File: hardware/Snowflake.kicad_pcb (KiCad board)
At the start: 2 copper layers, 70.5 x 79.8 mm, 41 parts, among them J1 Jumper, Q1 Q_DUAL_NMOS, SW1 SW_SPST, U1 Opamp_Single, U2 74HC595, U3 LM4041_1.2V

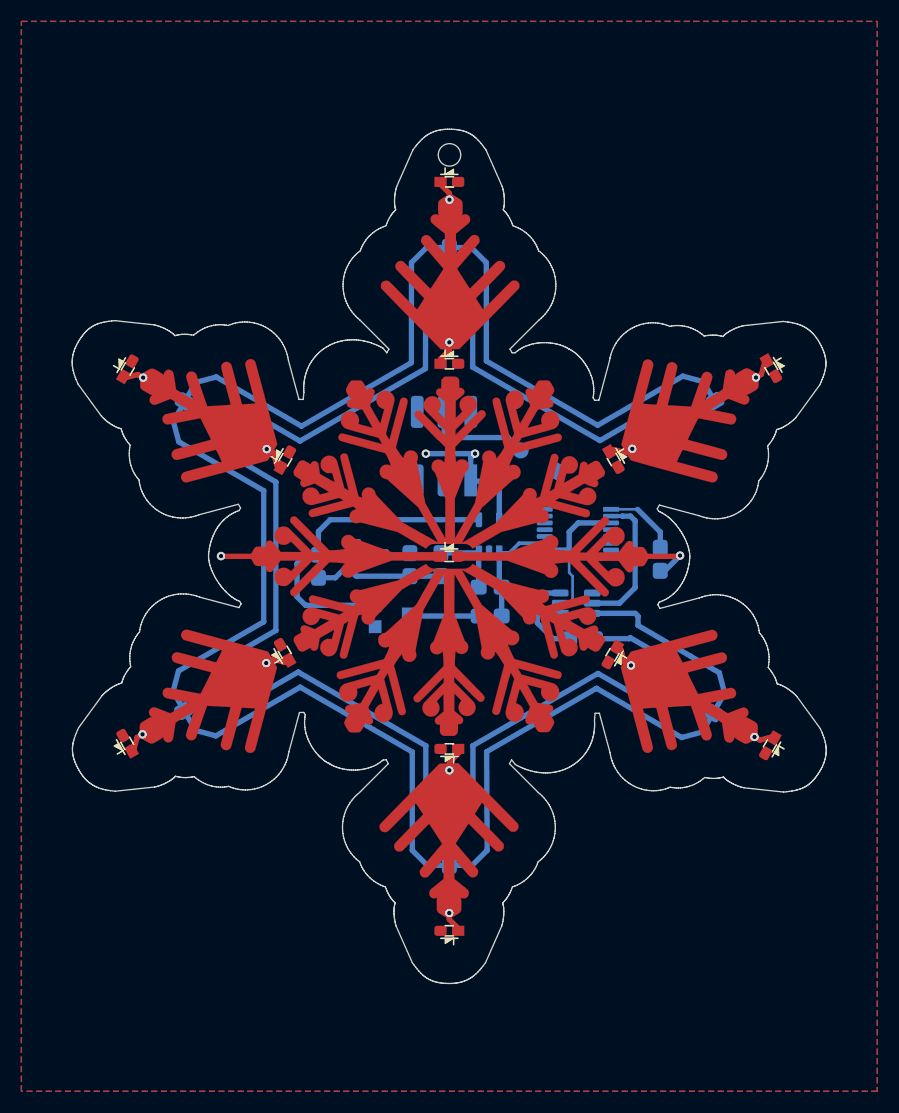
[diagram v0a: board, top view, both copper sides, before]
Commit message: Updated the Design to KiCad6 and made the track corners rounded
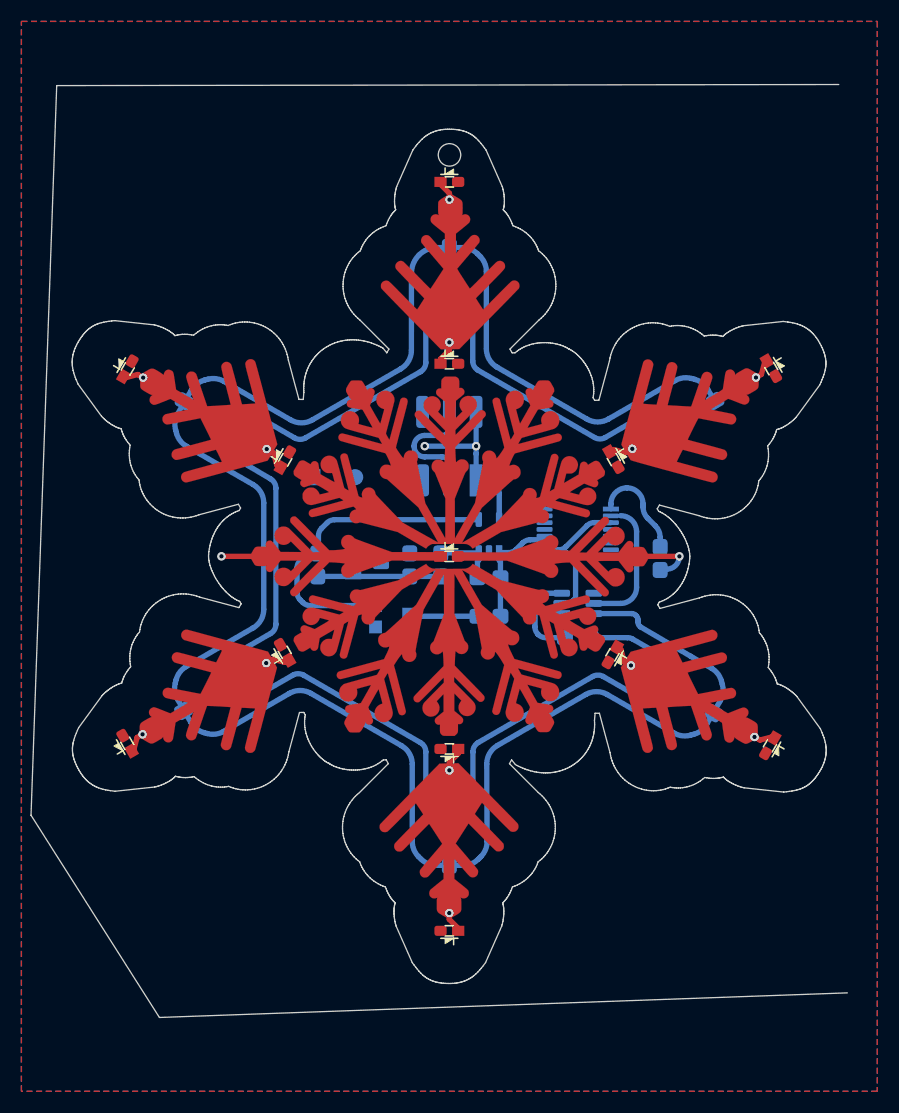
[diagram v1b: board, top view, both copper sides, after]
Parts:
- moved BT1 19.3 mm to (119.2, 109.6), turned to 180 degrees
- moved U3 1.07 mm to (122.3, 117.8)
- moved R2 0.88 mm to (133.7, 119.0)
- moved SW1 0.50 mm to (130.0, 106.7)
- moved J1 0.41 mm to (142.0, 124.6)
- moved C1 0.14 mm to (117.7, 117.8)
- moved Q1 0.14 mm to (142.0, 121.4)
- moved R1 0.11 mm to (133.7, 122.6)
- moved R4 0.08 mm to (149.7, 117.2)
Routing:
- net ROW1: track 211.0 -> 206.3 mm
- net VBAT: track 17.7 -> 21.0 mm
- net LED0: track 6.95 -> 9.61 mm
- net ROW0: track 169.4 -> 167.4 mm
- net Net-(BT1-Pad1): track 9.75 -> 11.4 mm
- net VBIAS: track 13.0 -> 11.6 mm
- net DRIVE_ROW0: track 14.2 -> 13.2 mm
- net Net-(R2-Pad2): track 6.77 -> 6.00 mm
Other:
- board size 70.5 x 79.8 mm -> 76.3 x 87.2 mm
- net class Default removed

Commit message: Fixed a bug, where I was sorting all the LEDs :S Removed all DRC rules Ready to fillet tracks
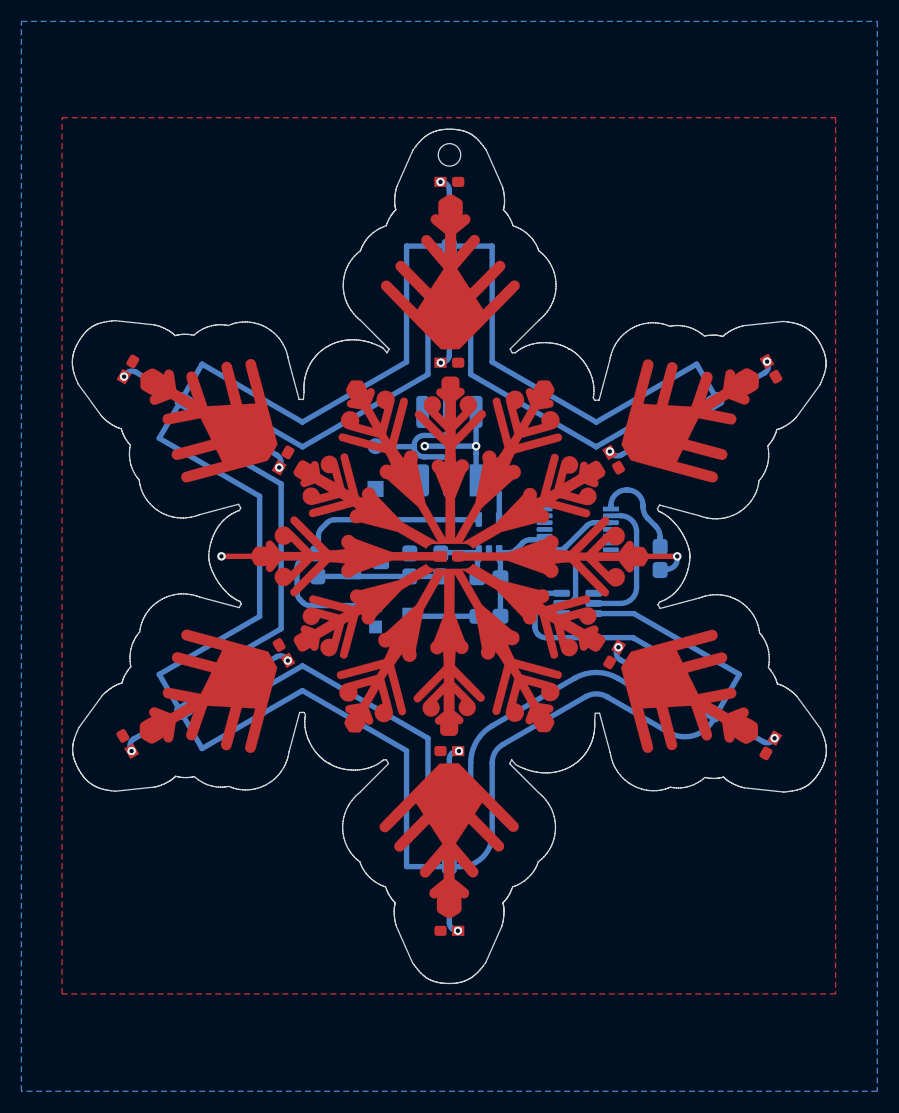
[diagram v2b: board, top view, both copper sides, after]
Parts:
- removed J1: Jumper, Snowflake:Jumper-0805
- BT1: value Battery -> Battery_Cell
- D1: renamed from D3; value White -> LED_Small_ALT; footprint Snowflake:0603_LED_HandSolder -> Snowflake:0603_LED_HandSolder_No_Silk
- D10: renamed from D17; value White -> LED_Small_ALT; footprint Snowflake:0603_LED_HandSolder -> Snowflake:0603_LED_HandSolder_No_Silk
- D11: renamed from D18; value White -> LED_Small_ALT; footprint Snowflake:0603_LED_HandSolder -> Snowflake:0603_LED_HandSolder_No_Silk
- D12: renamed from D21; value White -> LED_Small_ALT; footprint Snowflake:0603_LED_HandSolder -> Snowflake:0603_LED_HandSolder_No_Silk
- D13: renamed from D22; value White -> LED_Small_ALT; footprint Snowflake:0603_LED_HandSolder -> Snowflake:0603_LED_HandSolder_No_Silk
- D2: renamed from D1; value White -> LED_Small_ALT; footprint Snowflake:0603_LED_HandSolder -> Snowflake:0603_LED_HandSolder_No_Silk
- D3: renamed from D2; value White -> LED_Small_ALT; footprint Snowflake:0603_LED_HandSolder -> Snowflake:0603_LED_HandSolder_No_Silk
- D4: renamed from D5; value White -> LED_Small_ALT; footprint Snowflake:0603_LED_HandSolder -> Snowflake:0603_LED_HandSolder_No_Silk
- D5: renamed from D6; value White -> LED_Small_ALT; footprint Snowflake:0603_LED_HandSolder -> Snowflake:0603_LED_HandSolder_No_Silk
- D6: renamed from D9; value White -> LED_Small_ALT; footprint Snowflake:0603_LED_HandSolder -> Snowflake:0603_LED_HandSolder_No_Silk
- D7: renamed from D10; value White -> LED_Small_ALT; footprint Snowflake:0603_LED_HandSolder -> Snowflake:0603_LED_HandSolder_No_Silk
- D8: renamed from D13; value White -> LED_Small_ALT; footprint Snowflake:0603_LED_HandSolder -> Snowflake:0603_LED_HandSolder_No_Silk
- D9: renamed from D14; value White -> LED_Small_ALT; footprint Snowflake:0603_LED_HandSolder -> Snowflake:0603_LED_HandSolder_No_Silk
- R1: renamed from R5; value 6.8kΩ -> R_Small
- R10: renamed from R15; value XYZΩ -> R_Small
- R11: renamed from R16; value XYZΩ -> R_Small
- R12: renamed from R19; value XYZΩ -> R_Small
- R13: renamed from R20; value XYZΩ -> R_Small
- R14: renamed from R23; value XYZΩ -> R_Small
- R15: renamed from R24; value XYZΩ -> R_Small
- R16: renamed from R27; value XYZΩ -> R_Small
- R17: renamed from R28; value XYZΩ -> R_Small
- R2: renamed from R1; value 50kΩ -> R_Small
- R3: renamed from R2; value 35kΩ -> R_Small
- R4: renamed from R3; value 30kΩ -> R_Small
- R5: renamed from R4; value XYZΩ -> R_Small
- R6: renamed from R7; value XYZΩ -> R_Small
- R7: renamed from R8; value XYZΩ -> R_Small
- R8: renamed from R11; value XYZΩ -> R_Small
- R9: renamed from R12; value XYZΩ -> R_Small
- RV1: value 200kΩ -> R_POT_Small
- U1: value Opamp_Single -> Opamp_Single_MCP6001
- U2: renamed from U3; value LM4041_1.2V -> TL431D
- moved BT1 4.00 mm to (123.1, 108.7), turned to -90 degrees
- moved D8 0.20 mm to (130.0, 135.2)
- moved D12 0.16 mm to (114.5, 108.0)
- moved D6 0.16 mm to (145.4, 126.2)
- moved D10 0.11 mm to (114.5, 126.0)
- moved D2 0.10 mm to (130.0, 98.9)
- moved D13 0.06 mm to (100.0, 99.5)
- moved D4 0.06 mm to (145.4, 108.0)
- moved D5 0.05 mm to (160.1, 99.5)
- renumbered U2 to U3
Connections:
- RV1 pad 1: (no net) -> unconnected-(RV1-Pad1)
- U2 pad 3: (no net) -> unconnected-(U2-Pad3)
- U3 pad 10: DRIVE_ROW1 -> RESET
- U3 pad 15: (no net) -> unconnected-(U3-Pad15)
- U3 pad 4: (no net) -> unconnected-(U3-Pad4)
- U3 pad 5: (no net) -> unconnected-(U3-Pad5)
- U3 pad 6: (no net) -> unconnected-(U3-Pad6)
- U3 pad 7: (no net) -> unconnected-(U3-Pad7)
- U3 pad 9: (no net) -> unconnected-(U3-Pad9)
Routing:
- net ROW1: track 206.3 -> 220.8 mm
- net ROW0: track 167.4 -> 178.5 mm
- net Net-(BT1-Pad1): track 11.4 -> 15.1 mm
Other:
- board size 76.3 x 87.2 mm -> 70.5 x 79.8 mm

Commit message: Rounded the tracks!
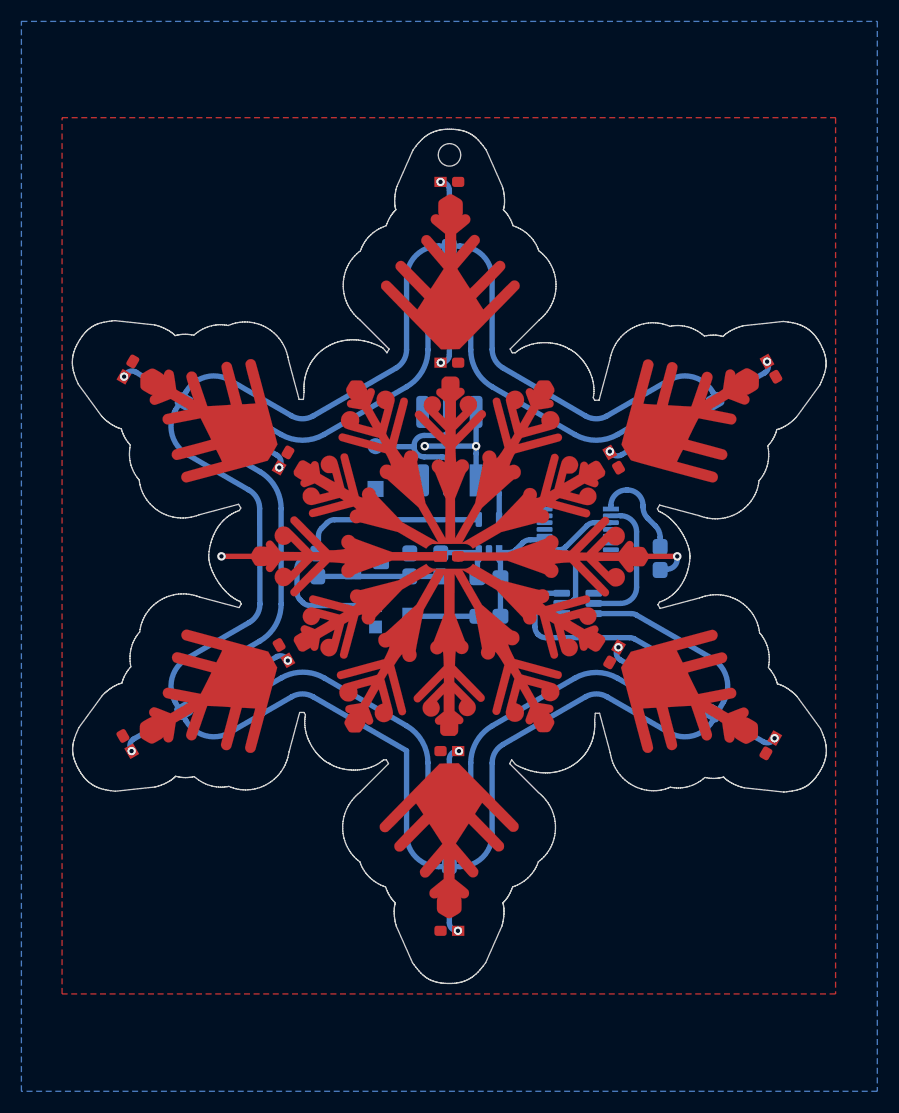
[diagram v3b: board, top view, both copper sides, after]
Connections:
- U3 pad 10: RESET -> DRIVE_ROW1
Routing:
- net ROW1: track 220.8 -> 206.5 mm
- net ROW0: track 178.5 -> 170.4 mm

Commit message: Discarded the idea of using AAA batteries and switched to CR2032s
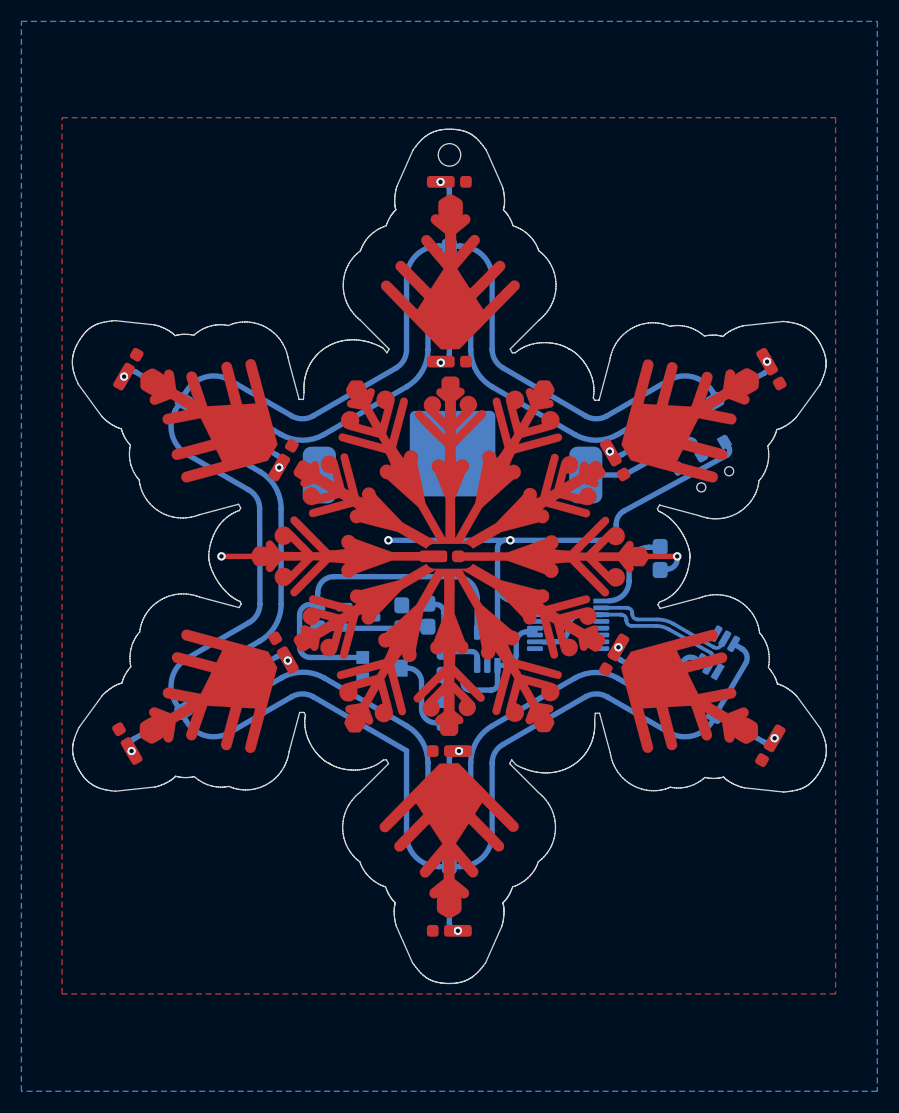
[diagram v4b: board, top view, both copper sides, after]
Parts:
- BT1: footprint Snowflake:Battery_Holder-AAA -> Snowflake:CR2032_Multicomp_MP000357_Alternative
- D1, D10, D11, D12, D13, D2, D3, D4, D5, D6, D7, D8, D9: footprint Snowflake:0603_LED_HandSolder_No_Silk -> Snowflake:4014_LED
- SW1: footprint Snowflake:Slide_Switch_JS202011SCQN -> Snowflake:Slider_Switch_C&K_AYZ0102AGRLC_SPDT_RightAngle
- moved SW1 25.0 mm to (154.8, 109.8), turned to -150 degrees
- moved Q1 13.8 mm to (155.0, 126.0), turned to 60 degrees
- moved U1 10.6 mm to (133.6, 125.7)
- moved R2 9.84 mm to (129.5, 131.5), turned to -90 degrees
- moved R3 9.04 mm to (129.5, 127.0), turned to 90 degrees
- moved U3 8.65 mm to (141.1, 123.4)
- moved BT1 7.32 mm to (130.3, 107.4), turned to 0 degrees
- moved RV1 5.00 mm to (123.7, 127.5)
- moved U2 4.97 mm to (121.5, 122.7)
- moved R1 4.91 mm to (125.5, 122.7)
- moved R4 4.85 mm to (128.0, 122.5)
- moved C1 4.85 mm to (117.7, 122.7)
- moved D1 0.70 mm to (129.3, 117.0)
- moved R11 0.23 mm to (155.8, 132.3)
- moved D2 0.10 mm to (130.0, 98.8)
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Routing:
- net VBAT: track 21.0 -> 49.8 mm
- net ROW0: track 170.4 -> 152.8 mm
- net ROW1: track 206.5 -> 196.5 mm
- net DRIVE_ROW1: track 13.9 -> 20.5 mm
- net CLK: track 11.3 -> 16.6 mm
- net Net-(R3-Pad2): track 6.02 -> 9.78 mm
- net Net-(BT1-Pad1): track 15.1 -> 12.4 mm
- net Net-(R2-Pad2): track 6.17 -> 8.34 mm
- net Net-(C1-Pad1): track 30.5 -> 32.5 mm
- net VBIAS: track 11.6 -> 10.8 mm
- net LED0: track 9.26 -> 8.74 mm
